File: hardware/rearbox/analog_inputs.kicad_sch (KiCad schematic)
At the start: 0 parts

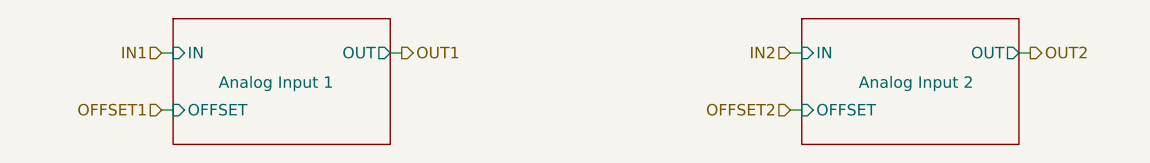
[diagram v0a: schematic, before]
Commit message: Place components on the PCB
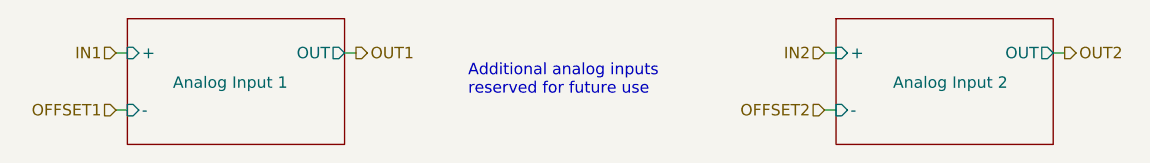
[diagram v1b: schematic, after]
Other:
- sheet Analog Input 1 ports: added +, -; removed IN, OFFSET
- sheet Analog Input 2 ports: added +, -; removed IN, OFFSET
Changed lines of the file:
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@@
   (title_block
     (title "Analog Inputs")
-    (date "2023-10-01")
+    (date "2023-11-02")
     (rev "${REVISION}")
     (company "Author: I. Kajdan")
     (comment 1 "Reviewer:")
   )
-  (wire (pts (xy 175.26 95.25) (xy 176.53 95.25))
+  (wire (pts (xy 179.07 95.25) (xy 180.34 95.25))
     (stroke (width 0) (type default))
   )
-  (wire (pts (xy 175.26 101.6) (xy 176.53 101.6))
+  (wire (pts (xy 179.07 101.6) (xy 180.34 101.6))
     (stroke (width 0) (type default))
   )
-  (wire (pts (xy 105.41 95.25) (xy 106.68 95.25))
+  (wire (pts (xy 100.33 95.25) (xy 101.6 95.25))
     (stroke (width 0) (type default))
   )
-  (wire (pts (xy 130.81 95.25) (xy 132.08 95.25))
+  (wire (pts (xy 125.73 95.25) (xy 127 95.25))
     (stroke (width 0) (type default))
   )
-  (wire (pts (xy 105.41 101.6) (xy 106.68 101.6))
+  (wire (pts (xy 100.33 101.6) (xy 101.6 101.6))
     (stroke (width 0) (type default))
   )
-  (wire (pts (xy 200.66 95.25) (xy 201.93 95.25))
+  (wire (pts (xy 204.47 95.25) (xy 205.74 95.25))
     (stroke (width 0) (type default))
   )
-  (hierarchical_label "OFFSET2" (shape input) (at 175.26 101.6 180) (fields_autoplaced)
+  (text_box "Additional analog inputs reserved for future use"
+    (at 138.43 95.25 0) (size 27.94 6.35)
+    (stroke (width -0.0001) (type default))
+    (fill (type none))
+    (effects (font (size 1.27 1.27)) (justify left top))
+  )
+  (hierarchical_label "OFFSET2" (shape input) (at 179.07 101.6 180) (fields_autoplaced)
     (effects (font (size 1.27 1.27)) (justify right))
   )
-  (hierarchical_label "OFFSET1" (shape input) (at 105.41 101.6 180) (fields_autoplaced)
+  (hierarchical_label "OFFSET1" (shape input) (at 100.33 101.6 180) (fields_autoplaced)
     (effects (font (size 1.27 1.27)) (justify right))
   )
-  (hierarchical_label "IN2" (shape input) (at 175.26 95.25 180) (fields_autoplaced)
+  (hierarchical_label "IN2" (shape input) (at 179.07 95.25 180) (fields_autoplaced)
     (effects (font (size 1.27 1.27)) (justify right))
   )
-  (hierarchical_label "OUT2" (shape output) (at 201.93 95.25 0) (fields_autoplaced)
+  (hierarchical_label "OUT2" (shape output) (at 205.74 95.25 0) (fields_autoplaced)
     (effects (font (size 1.27 1.27)) (justify left))
   )
-  (hierarchical_label "IN1" (shape input) (at 105.41 95.25 180) (fields_autoplaced)
+  (hierarchical_label "IN1" (shape input) (at 100.33 95.25 180) (fields_autoplaced)
     (effects (font (size 1.27 1.27)) (justify right))
   )
-  (hierarchical_label "OUT1" (shape output) (at 132.08 95.25 0) (fields_autoplaced)
+  (hierarchical_label "OUT1" (shape output) (at 127 95.25 0) (fields_autoplaced)
     (effects (font (size 1.27 1.27)) (justify left))
   )
-  (sheet (at 106.68 91.44) (size 24.13 13.97)
+  (sheet (at 101.6 91.44) (size 24.13 13.97)
     (stroke (width 0.1524) (type solid))
     (fill (color 0 0 0 0.0000))
-    (property "Sheetname" "Analog Input 1" (at 118.11 97.79 0)
+    (property "Sheetname" "Analog Input 1" (at 113.03 97.79 0)
       (effects (font (size 1.27 1.27)) (justify top))
     )
-    (property "Sheetfile" "analog_input.kicad_sch" (at 106.68 108.5346 0)
+    (property "Sheetfile" "analog_input.kicad_sch" (at 101.6 108.5346 0)
       (effects (font (size 1.27 1.27)) (justify left top) hide)
     )
-    (pin "IN" input (at 106.68 95.25 180)
+    (pin "+" input (at 101.6 95.25 180)
       (effects (font (size 1.27 1.27)) (justify left))
     )
-    (pin "OUT" output (at 130.81 95.25 0)
+    (pin "OUT" output (at 125.73 95.25 0)
       (effects (font (size 1.27 1.27)) (justify right))
     )
-    (pin "OFFSET" input (at 106.68 101.6 180)
+    (pin "-" input (at 101.6 101.6 180)
       (effects (font (size 1.27 1.27)) (justify left))
     )
@@
     )
   )
-  (sheet (at 176.53 91.44) (size 24.13 13.97)
+  (sheet (at 180.34 91.44) (size 24.13 13.97)
     (stroke (width 0.1524) (type solid))
     (fill (color 0 0 0 0.0000))
-    (property "Sheetname" "Analog Input 2" (at 189.23 97.79 0)
+    (property "Sheetname" "Analog Input 2" (at 193.04 97.79 0)
       (effects (font (size 1.27 1.27)) (justify top))
     )
-    (property "Sheetfile" "analog_input.kicad_sch" (at 176.53 108.5346 0)
+    (property "Sheetfile" "analog_input.kicad_sch" (at 180.34 108.5346 0)
       (effects (font (size 1.27 1.27)) (justify left top) hide)
     )
-    (pin "IN" input (at 176.53 95.25 180)
+    (pin "+" input (at 180.34 95.25 180)
       (effects (font (size 1.27 1.27)) (justify left))
     )
-    (pin "OUT" output (at 200.66 95.25 0)
+    (pin "OUT" output (at 204.47 95.25 0)
       (effects (font (size 1.27 1.27)) (justify right))
     )
-    (pin "OFFSET" input (at 176.53 101.6 180)
+    (pin "-" input (at 180.34 101.6 180)
       (effects (font (size 1.27 1.27)) (justify left))
     )

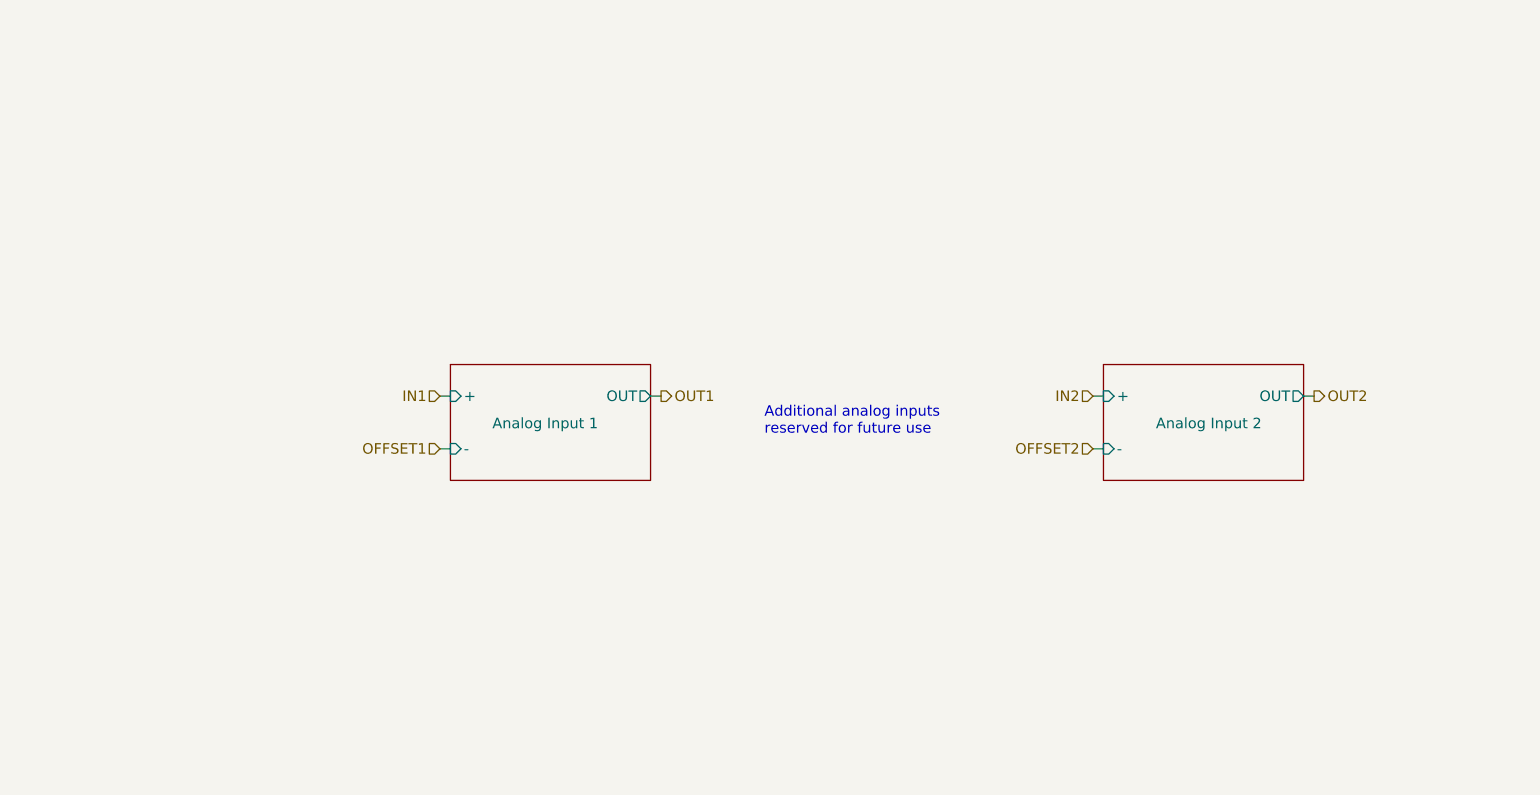
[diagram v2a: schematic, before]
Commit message: Fix measurement bridges polarity
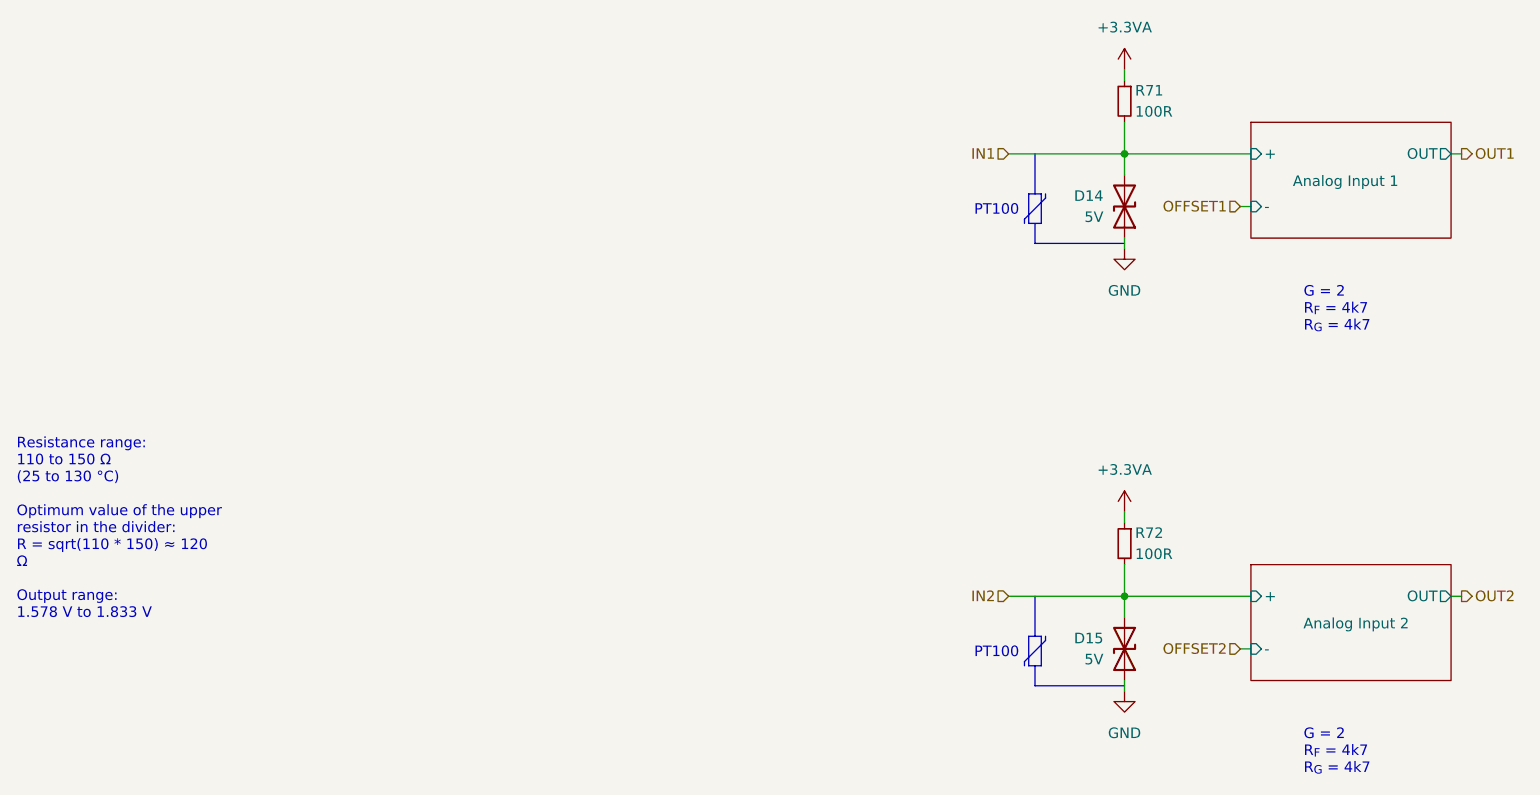
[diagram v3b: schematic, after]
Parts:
- added D14, D15: 5V, Diode_SMD:D_SOD-523, symbol Device:D_TVS
- added R71, R72: 100R, Resistor_SMD:R_0603_1608Metric, symbol Device:R_Small
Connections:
- net IN1: now also D14.2 (A2), R71.2
- net IN2: now also D15.2 (A2), R72.2
- new net +3.3VA: R71.1, R72.1
- new net GND: D14.1 (A1), D15.1 (A1)
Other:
- note added: "G = 2 R_{F} = 4k7 R_{G} = 4k7"
- note added: "PT100"
- title: Analog Inputs -> Oil Temperature Sensors
